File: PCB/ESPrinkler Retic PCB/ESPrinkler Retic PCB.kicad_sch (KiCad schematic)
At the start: 0 parts

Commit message: Begin work on PCB design
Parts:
- added C1: 22nF, symbol Device:C_Small
- added C2: 680uF, symbol Device:C_Polarized
- added C3: 10uF, symbol Device:C
- added C4: 22uF, symbol Device:C_Polarized
- added D1: Generic_Triac_A1A2G, symbol Triac_Thyristor:Generic_Triac_A1A2G
- added D2: D_TVS, symbol Device:D_TVS
- added D3: ~, symbol Device:D_Bridge_+AA-
- added D4: D_Schottky, symbol Device:D_Schottky
- added F1: Polyfuse, symbol Device:Polyfuse
- added J1, J2: Conn_01x02, symbol Connector_Generic:Conn_01x02
- added L1: 33uH, symbol Device:L
- added R1: 68R, symbol Device:R_Small
- added R2: 82R, symbol Device:R_Small
- added R3: 120R, symbol Device:R_Small
- added U1: MOC3063S, Package_DIP:SMDIP-6_W9.53mm, symbol Relay_SolidState:MOC3063M
- added U2: LM2596S-5, Package_TO_SOT_SMD:TO-263-5_TabPin3, symbol Regulator_Switching:LM2596S-5
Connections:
- new net: D4.1 (K), L1.1, U2.2 (OUT)
- new net: D1.3 (G), R3.2, U1.4
- new net: R1.2, U1.6
- new net: D1.2 (A2), D2.1 (A1), J2.2 (Pin_2), R2.1
- new net: C1.1, R1.1, R2.2
- new net +5V: C4.1, L1.2, U2.4 (FB)
- new net GND: C2.2, C3.2, C4.2, D3.4 (-), D4.2 (A), U2.3 (GND), U2.5 (~{ON}/OFF)
- new net LIVE: D2.2 (A2), D3.2, F1.1, J1.1 (Pin_1), J2.1 (Pin_1)
- new net NEUT: C1.2, D1.1 (A1), D3.3, F1.2, J1.2 (Pin_2), R3.1
- new net VCC: C2.1, C3.1, D3.1 (+), U2.1 (VIN)
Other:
- note added: "https://www.st.com/resource/en/application_note/an5114-controlling-a-triac-with-a-phototriac-stmicroelectronics.pdf"

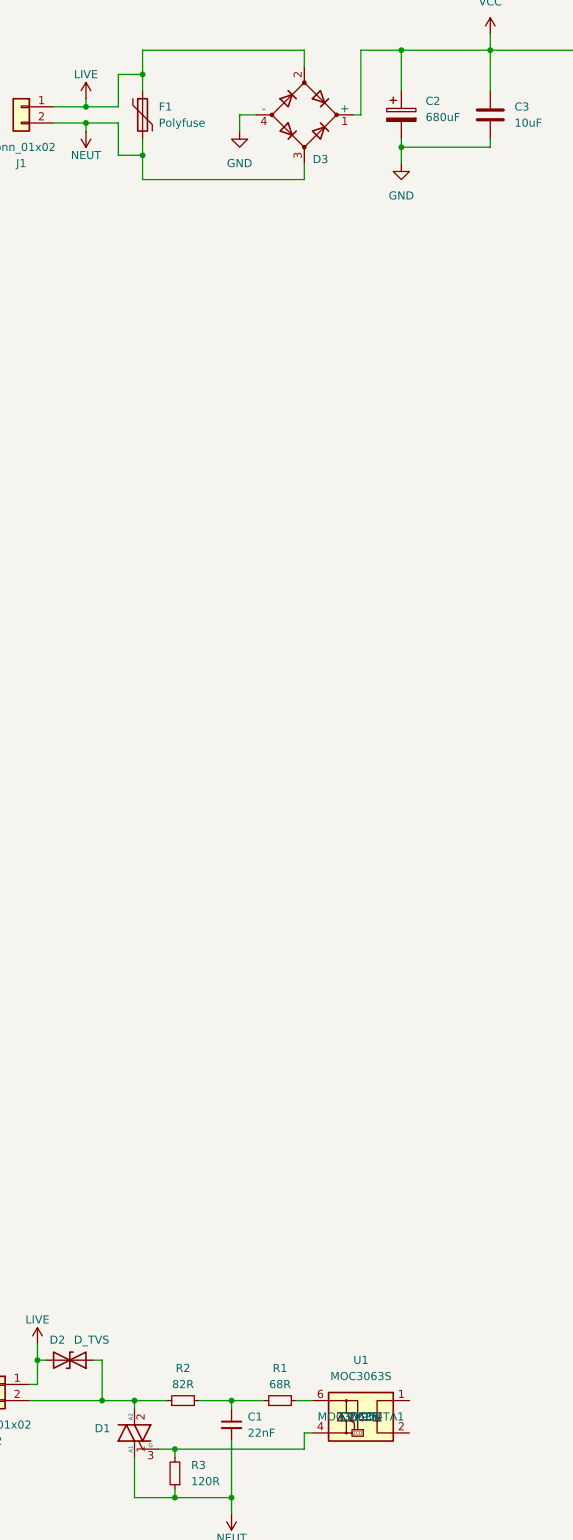
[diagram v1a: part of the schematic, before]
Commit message: Choose parts for components
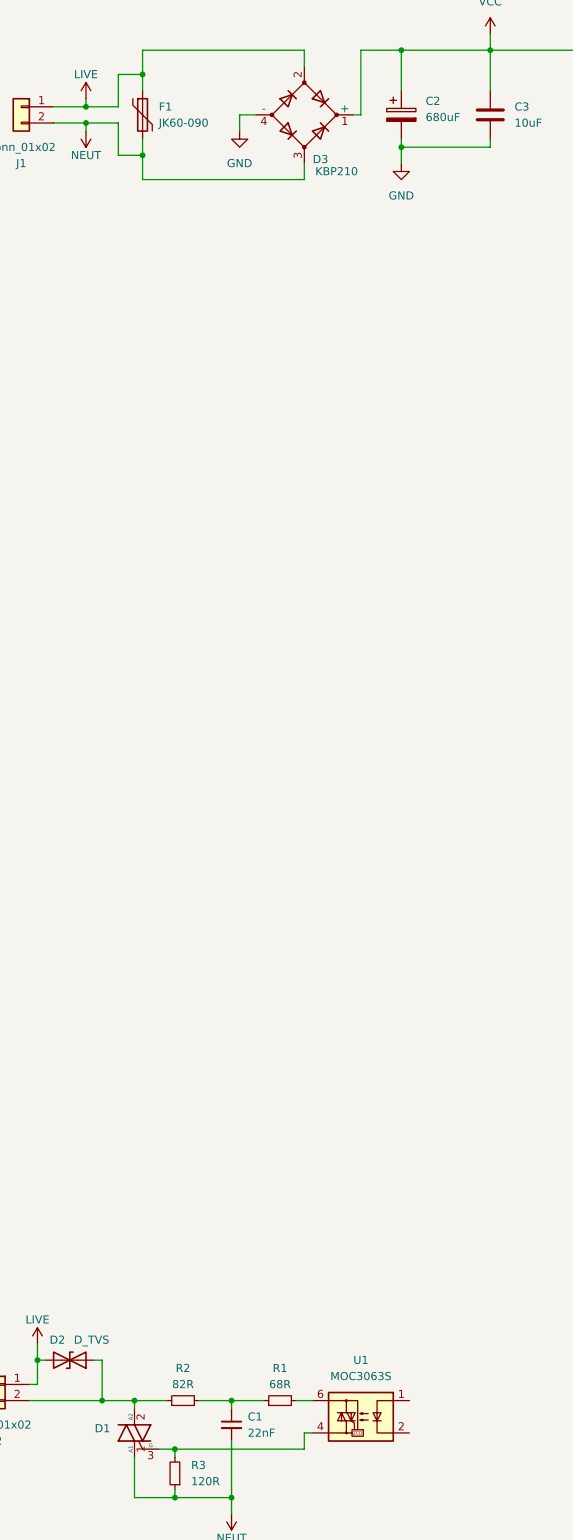
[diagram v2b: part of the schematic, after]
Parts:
- D3: value ~ -> KBP210; footprint (none) -> Diode_THT:Diode_Bridge_Vishay_KBPM; LCSC Part Number (none) -> C3081; Manufacturer (none) -> MDD(Microdiode Semiconductor); Manufacturer Part Number (none) -> KBP210
- F1: value Polyfuse -> JK60-090; footprint (none) -> Fuse:Fuse_Bourns_MF-RHT500; LCSC Part Number (none) -> C369087; Manufacturer (none) -> Jinrui Electronic Materials Co.; Manufacturer Part Number (none) -> JK60-090
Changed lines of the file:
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@@
 			)
 		)
-		(property "Value" "~"
-			(at 74.93 45.72 0)
-			(effects
-				(font
-					(size 1.27 1.27)
-				)
-			)
-		)
-		(property "Footprint" ""
+		(property "Value" "KBP210"
+			(at 76.2 45.72 0)
+			(effects
+				(font
+					(size 1.27 1.27)
+				)
+			)
+		)
+		(property "Footprint" "Diode_THT:Diode_Bridge_Vishay_KBPM"
 			(at 71.12 36.83 0)
 			(effects
@@
 			)
 		)
-		(property "Datasheet" "~"
+		(property "Datasheet" "https://www.lcsc.com/datasheet/lcsc_datasheet_2411211950_MDD-Microdiode-Semiconductor-KBP210_C3081.pdf"
 			(at 71.12 36.83 0)
 			(effects
@@
 			)
 		)
-		(property "Manufacturer" ""
+		(property "Manufacturer" "MDD(Microdiode Semiconductor)"
 			(at 71.12 36.83 0)
 			(effects
@@
 					(size 1.27 1.27)
 				)
-			)
-		)
-		(property "Manufacturer Part Number" ""
+				(hide yes)
+			)
+		)
+		(property "Manufacturer Part Number" "KBP210"
 			(at 71.12 36.83 0)
 			(effects
@@
 					(size 1.27 1.27)
 				)
-			)
-		)
-		(property "LCSC Part Number" ""
+				(hide yes)
+			)
+		)
+		(property "LCSC Part Number" "C3081"
 			(at 71.12 36.83 0)
 			(effects
@@
 					(size 1.27 1.27)
 				)
+				(hide yes)
 			)
 		)
@@
 					(size 1.27 1.27)
 				)
+				(hide yes)
 			)
 		)
@@
 					(size 1.27 1.27)
 				)
+				(hide yes)
 			)
 		)
@@
 					(size 1.27 1.27)
 				)
+				(hide yes)
 			)
 		)
@@
 					(size 1.27 1.27)
 				)
+				(hide yes)
 			)
 		)
@@
 					(size 1.27 1.27)
 				)
+				(hide yes)
 			)
 		)
@@
 					(size 1.27 1.27)
 				)
+				(hide yes)
 			)
 		)
@@
 			)
 		)
-		(property "Value" "Polyfuse"
+		(property "Value" "JK60-090"
 			(at 48.26 38.0999 0)
 			(effects
@@
 			)
 		)
-		(property "Footprint" ""
+		(property "Footprint" "Fuse:Fuse_Bourns_MF-RHT500"
 			(at 46.99 41.91 0)
 			(effects
@@
 			)
 		)
-		(property "Datasheet" "~"
+		(property "Datasheet" "https://www.lcsc.com/datasheet/lcsc_datasheet_2304140030_Jinrui-Electronic-Materials-Co--JK60-090_C369087.pdf"
 			(at 45.72 36.83 0)
 			(effects
@@
 			)
 		)
-		(property "Manufacturer" ""
+		(property "Manufacturer" "Jinrui Electronic Materials Co."
 			(at 45.72 36.83 0)
 			(effects
@@
 					(size 1.27 1.27)
 				)
-			)
-		)
-		(property "Manufacturer Part Number" ""
+				(hide yes)
+			)
+		)
+		(property "Manufacturer Part Number" "JK60-090"
 			(at 45.72 36.83 0)
 			(effects
@@
 					(size 1.27 1.27)
 				)
-			)
-		)
-		(property "LCSC Part Number" ""
+				(hide yes)
+			)
+		)
+		(property "LCSC Part Number" "C369087"
 			(at 45.72 36.83 0)
 			(effects
@@
 					(size 1.27 1.27)
 				)
-			)
-		)
+				(hide yes)
+			)
+		)

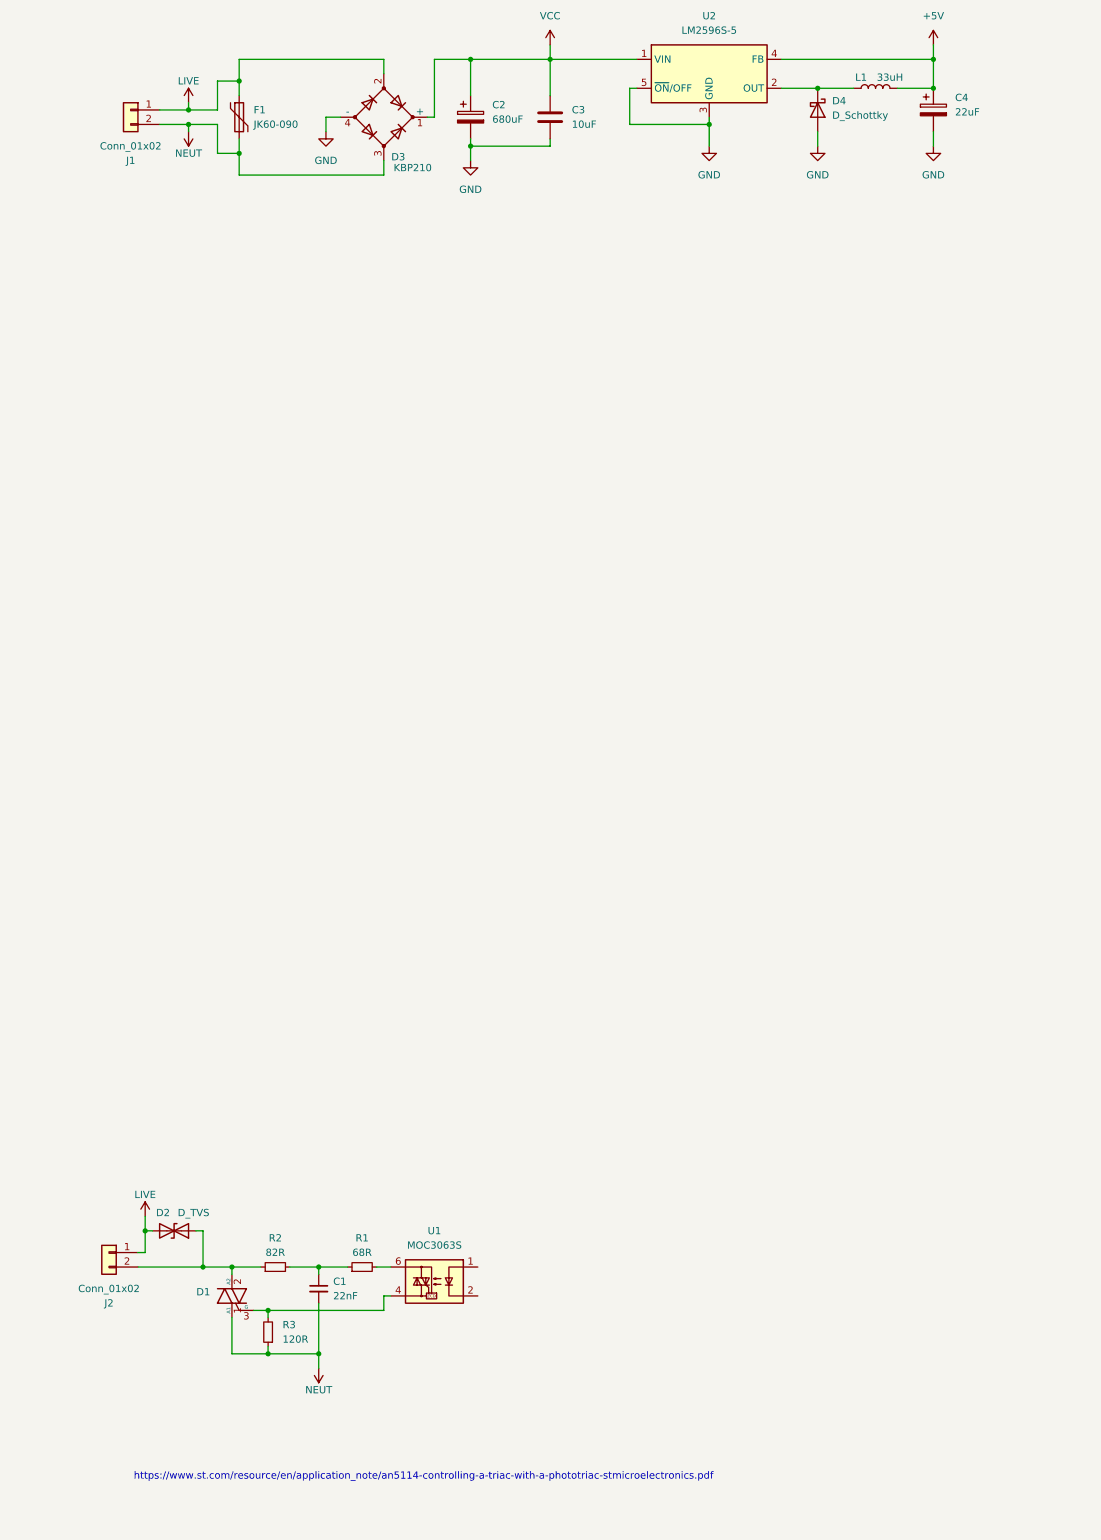
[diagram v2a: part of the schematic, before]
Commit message: Continue with parts selection for components
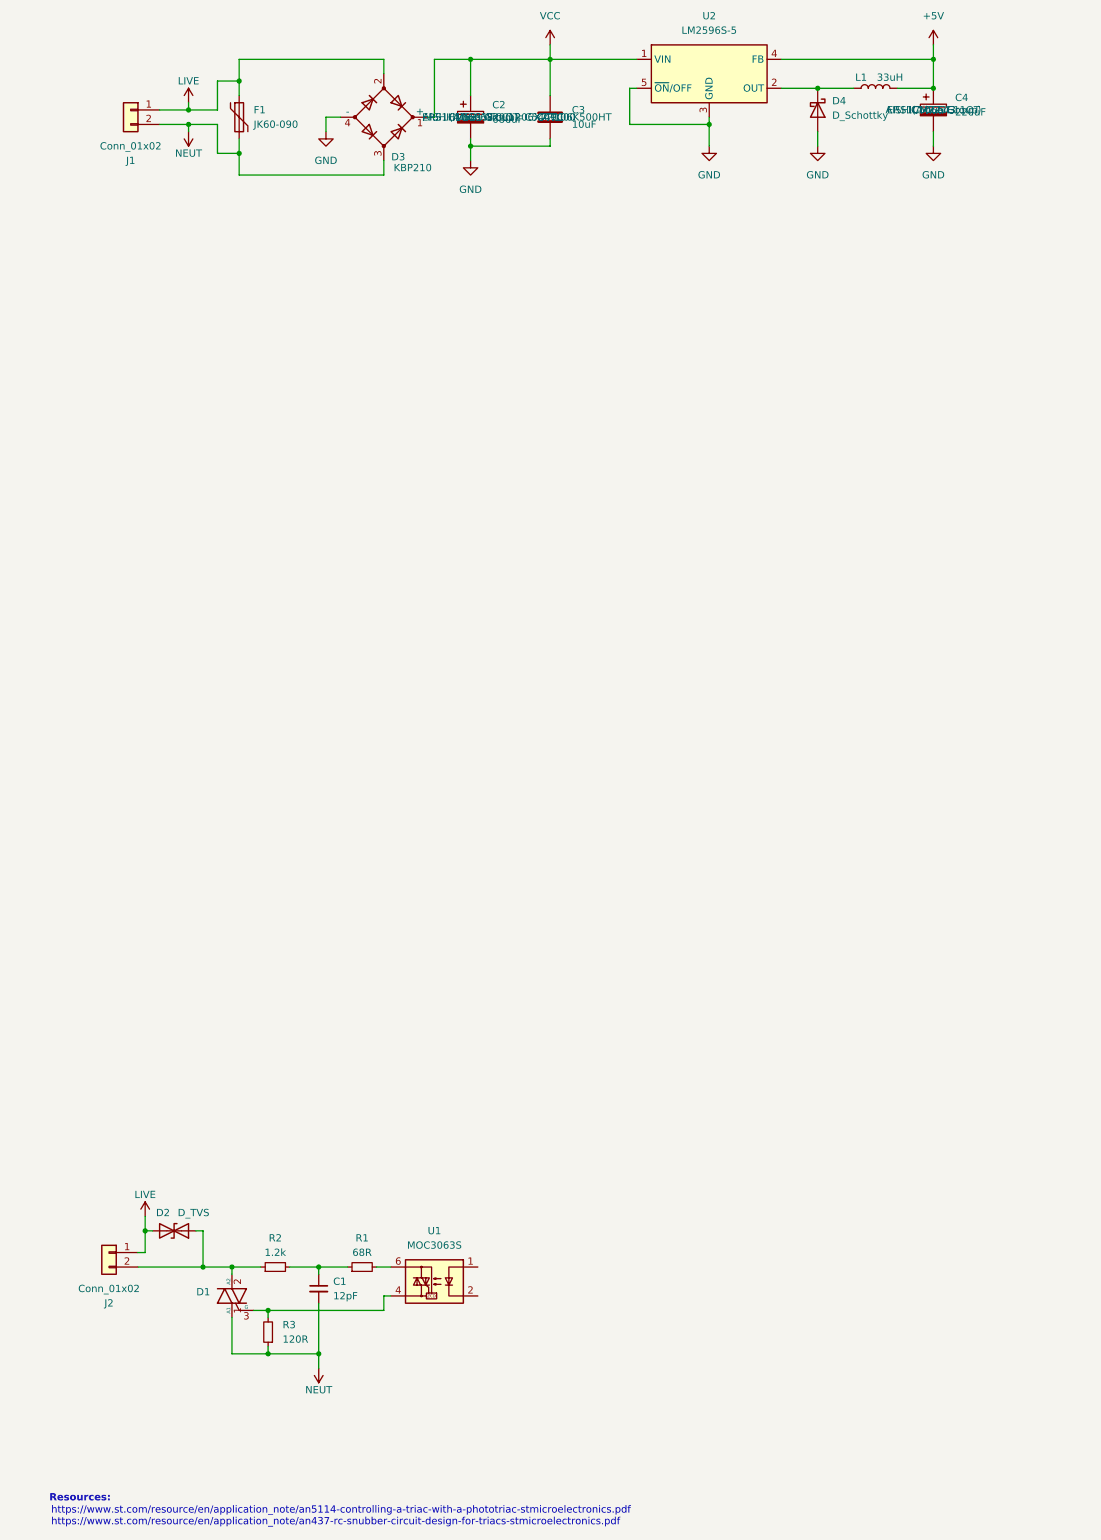
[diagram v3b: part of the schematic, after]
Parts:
- C1: value 22nF -> 12pF
- C2: footprint (none) -> Capacitor_THT:CP_Radial_D12.5mm_P5.00mm; LCSC Part Number (none) -> C106668; Manufacturer (none) -> AISHI(Aihua Group); Manufacturer Part Number (none) -> ERS1HM681W20OT
- C3: footprint (none) -> Capacitor_SMD:C_1206_3216Metric; LCSC Part Number (none) -> C5449000; Manufacturer (none) -> CCTC; Manufacturer Part Number (none) -> TCC1206X7R106K500HT
- C4: value 22uF -> 220uF; footprint (none) -> Capacitor_THT:CP_Radial_D6.3mm_P2.50mm; LCSC Part Number (none) -> C106643; Manufacturer (none) -> AISHI(Aihua Group); Manufacturer Part Number (none) -> ERS1CM221E11OT
- R2: value 82R -> 1.2k
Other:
- note added: "Resources:"
- note added: "https://www.st.com/resource/en/application_note/an5114-controlling-a-triac-with-a-phototriac-stmicroelectronics.pdf https://www.st.com/resource/en/application_note/an437-rc-snubber-circuit-design-for-triacs-stmicroelectronics.pdf"
- note removed: "https://www.st.com/resource/en/application_note/an5114-controlling-a-triac-with-a-phototriac-stmicroelectronics.pdf"
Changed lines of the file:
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@@
 		(rev "1.0")
 	)
-	(text "https://www.st.com/resource/en/application_note/an5114-controlling-a-triac-with-a-phototriac-stmicroelectronics.pdf"
+	(text "https://www.st.com/resource/en/application_note/an5114-controlling-a-triac-with-a-phototriac-stmicroelectronics.pdf\nhttps://www.st.com/resource/en/application_note/an437-rc-snubber-circuit-design-for-triacs-stmicroelectronics.pdf"
 		(exclude_from_sim no)
-		(at 78.105 275.59 0)
+		(at 12.7 282.575 0)
 		(effects
 			(font
 				(size 1.27 1.27)
 			)
+			(justify left)
+		)
+	)
+	(text "Resources:"
+		(exclude_from_sim no)
+		(at 17.78 279.4 0)
+		(effects
+			(font
+				(size 1.27 1.27)
+				(thickness 0.254)
+				(bold yes)
+			)
 		)
 	)
@@
 			)
 		)
-		(property "Footprint" ""
+		(property "Footprint" "Capacitor_THT:CP_Radial_D12.5mm_P5.00mm"
 			(at 87.3252 40.64 0)
 			(effects
@@
 			)
 		)
-		(property "LCSC Part Number" ""
+		(property "LCSC Part Number" "C106668"
+			(at 86.36 36.83 0)
+			(effects
+				(font
+					(size 1.27 1.27)
+				)
+			)
+		)
+		(property "Manufacturer" "AISHI(Aihua Group)"
+			(at 86.36 36.83 0)
+			(effects
+				(font
+					(size 1.27 1.27)
+				)
+			)
+		)
+		(property "Manufacturer Part Number" "ERS1HM681W20OT"
 			(at 86.36 36.83 0)
 			(effects
@@
 			)
 		)
-		(property "Value" "82R"
+		(property "Value" "1.2k"
 			(at 52.07 236.22 90)
 			(effects
@@
 			)
 		)
-		(property "Value" "22nF"
+		(property "Value" "12pF"
 			(at 62.23 243.8462 0)
 			(effects
@@
 			)
 		)
-		(property "Value" "22uF"
+		(property "Value" "220uF"
 			(at 171.45 35.9409 0)
 			(effects
@@
 			)
 		)
-		(property "Footprint" ""
+		(property "Footprint" "Capacitor_THT:CP_Radial_D6.3mm_P2.50mm"
 			(at 168.6052 39.37 0)
 			(effects
@@
 			)
 		)
-		(property "LCSC Part Number" ""
+		(property "LCSC Part Number" "C106643"
+			(at 167.64 35.56 0)
+			(effects
+				(font
+					(size 1.27 1.27)
+				)
+			)
+		)
+		(property "Manufacturer" "AISHI(Aihua Group)"
+			(at 167.64 35.56 0)
+			(effects
+				(font
+					(size 1.27 1.27)
+				)
+			)
+		)
+		(property "Manufacturer Part Number" "ERS1CM221E11OT"
 			(at 167.64 35.56 0)
 			(effects
@@
 			)
 		)
-		(property "Footprint" ""
+		(property "Footprint" "Capacitor_SMD:C_1206_3216Metric"
 			(at 101.2952 40.64 0)
 			(effects
@@
 			)
 		)
+		(property "LCSC Part Number" "C5449000"
+			(at 100.33 36.83 0)
+			(effects
+				(font
+					(size 1.27 1.27)
+				)
+			)
+		)
+		(property "Manufacturer" "CCTC"
+			(at 100.33 36.83 0)
+			(effects
+				(font
+					(size 1.27 1.27)
+				)
+			)
+		)
+		(property "Manufacturer Part Number" "TCC1206X7R106K500HT"
+			(at 100.33 36.83 0)
+			(effects
+				(font
+					(size 1.27 1.27)
+				)
+			)
+		)
